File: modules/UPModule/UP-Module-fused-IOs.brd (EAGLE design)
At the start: 48.6 x 50.4 mm, 137 parts, among them IC1 LPC1115, IC100 BD9G101, IC2 ESDA5V3L, IC302 ESDA5V3L, IC303 ESDA5V3L, IC304 ESDA5V3L, IC401 ESDA5V3L, IC402 ESDA5V3L, IC403 ESDA5V3L, IC404 ESDA5V3L, Q2 ASFL, T1 BC856, T2 BCP52, T3 BC847, X1 EIB, X2 B7B-PH-K-S, X3 B8B-PH-K-S

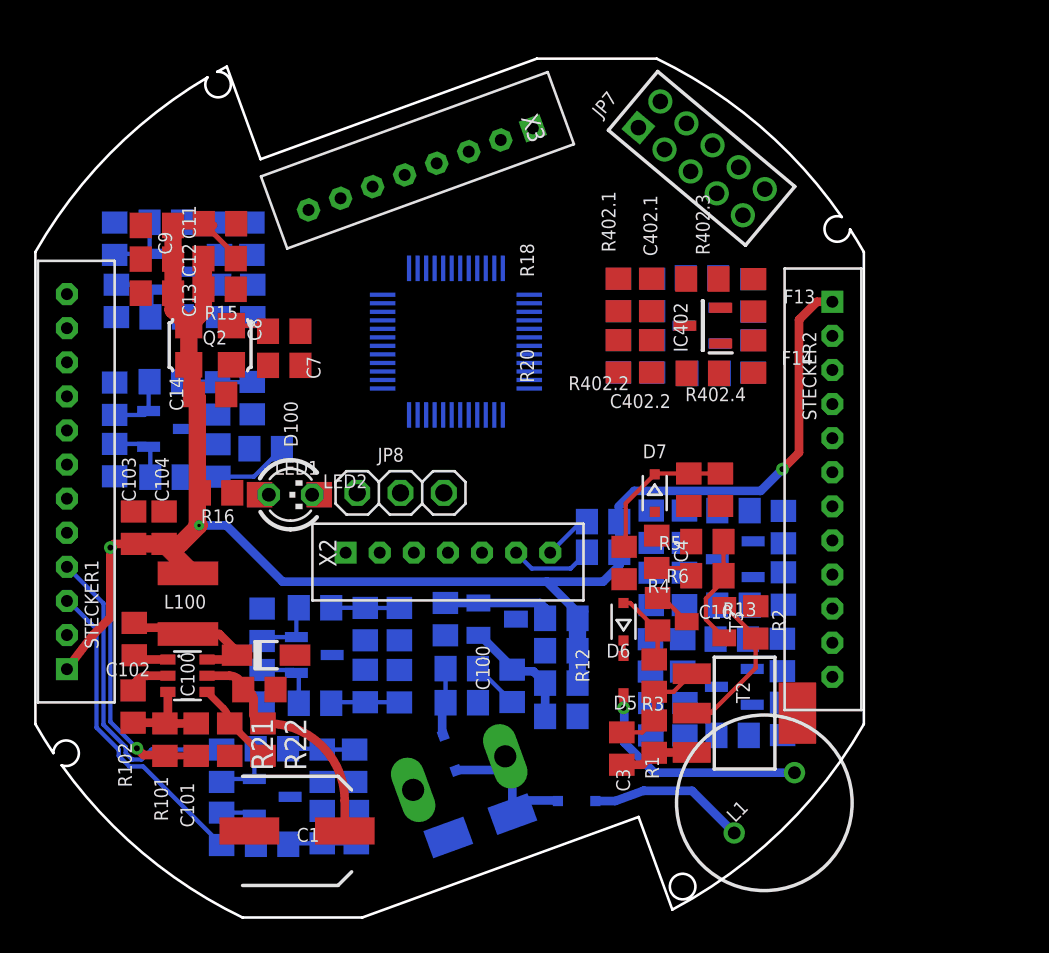
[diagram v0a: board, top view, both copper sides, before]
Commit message: Update of UP Module with fused IOs
Completely changed how IOs will be protected. EEPROM and cropty IC added.
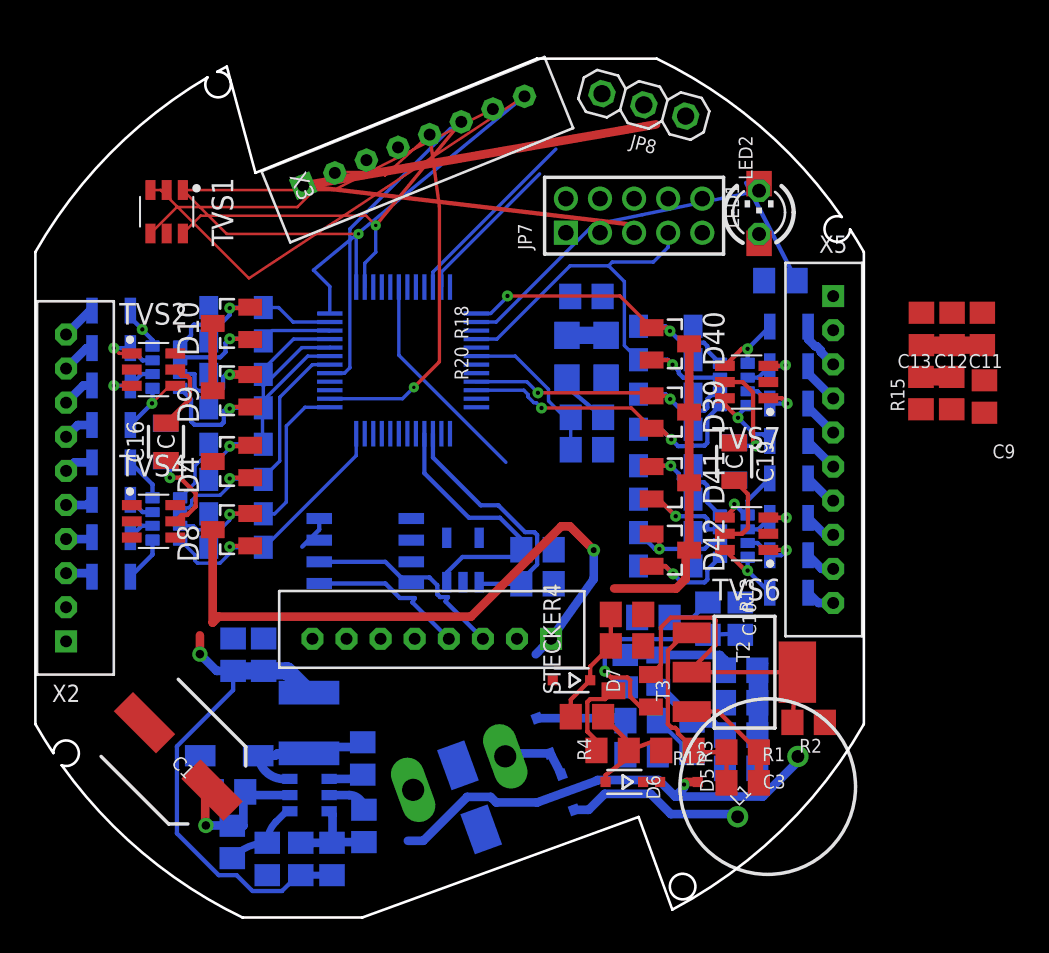
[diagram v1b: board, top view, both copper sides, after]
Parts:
- removed C302.1, C302.2, C303.1, C303.2, C304.1, C304.2, C304.3, C304.4, C401.1, C401.2, C402.1, C402.2, C403.1, C403.2, C404.1, C404.2: 10nF/50V, rcl:C0805
- removed F13, F14, F15, F16, F3, F4, F5: BSMD0805-005-33V, rcl:R0805
- removed IC2, IC302, IC303, IC304, IC401, IC402, IC403, IC404: ESDA5V3L, SamacSys_Parts:SOT105P242X150-3N
- removed R302.1, R302.2, R303.1, R303.2, R304.1, R304.2, R304.5, R304.6, R401.1, R401.2, R402.1, R402.2, R403.1, R403.2, R404.1, R404.2: 1M, rcl:R0805
- removed R302.3, R302.4, R303.3, R303.4, R304.3, R304.4, R304.7, R304.8, R401.3, R401.4, R402.3, R402.4, R403.3, R403.4, R404.3, R404.4: 1k, rcl:R0805
- removed STECKER1, STECKER2: B12B-PH-K-S, con-JST PH:B12B-PH-K-S
- added C16, C17, C19, C20: 100nF, MyRCL:C0805
- added D10, D39, D4, D40, D41, D42, D8, D9: BAT54C, diode:SOT23
- added D13, D14, D15, D16, D18, D19, D20, D21, D31, D32, D33, D34, D35, D36, D37, D38: DDZ9684 (3V3), Diode:SODFL3718X115
- added F1, F19, F20, F21, F22, F23, F24: (no value), MyFuse:F0805
- added IC5: ATAES132A-SHEQ-T, SamacSys_Parts:SOIC127P600X175-8N
- added R19, R23, R25, R26: YC164-JR-0733RL, Resistor Array:YC164-JR-0733RL
- added STECKER4: B8B-PH-K-S, con-JST PH:B8B-PH-K-S
- added TVS1, TVS2, TVS4, TVS6, TVS7: USBLC6-4SC6, usblc6:SOT-23-6L
- added U1: (no value), microbuilder:SOT23-5
- added X5: B10B-PH-KL, con-JST PH:B10B-PH-K-S
- F10, F11, F12, F17, F18, F6, F7, F8, F9: value BSMD0805-005-33V -> (none); device rcl:R0805 -> MyFuse:F0805
- X2: value B7B-PH-K-S -> B10B-PH-KL; device con-JST PH:B7B-PH-K-S -> con-JST PH:B10B-PH-K-S
- moved C11 48.8 mm to (55.4, 34.7), turned to 270 degrees
- moved C12 46.8 mm to (53.6, 34.7), turned to 270 degrees
- moved C9 46.0 mm to (55.5, 30.8), turned to 270 degrees
- moved C13 44.9 mm to (51.8, 34.7), turned to 270 degrees
- moved R14 43.7 mm to (53.5, 31.0), turned to 90 degrees
- moved R15 41.6 mm to (51.8, 31.0), turned to 90 degrees
- moved F11 39.5 mm to (4.25, 24.7), turned to 180 degrees
- moved F12 38.2 mm to (4.25, 26.9), turned to 180 degrees
- moved R16 35.4 mm to (43.5, 37.6), flipped to the bottom
- moved LED1 32.1 mm to (42.3, 41.5), turned to 0 degrees
- moved LED2 32.1 mm to (42.2, 41.6), turned to 90 degrees
- moved F7 28.9 mm to (4.25, 33.6), turned to 180 degrees
- moved F8 27.5 mm to (4.25, 35.8), turned to 180 degrees
- moved JP8 26.9 mm to (35.5, 47.9), turned to 165 degrees
- moved C14 22.8 mm to (32.1, 36.6), flipped to the bottom
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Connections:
- removed net C1_P10: F10.2, STECKER1.10
- removed net C1_P10_F: F10.1, IC2.2, R304.8.1
- removed net C1_P3: F7.2, STECKER1.3
- removed net C1_P3_F: F7.1, IC304.1, R304.3.1
- removed net C1_P4: F8.2, STECKER1.4
- removed net C1_P4_F: F8.1, IC304.2, R304.4.1
- removed net C1_P5: F5.2, STECKER1.5
- removed net C1_P5_F: F5.1, IC303.1, R303.3.1
- removed net C1_P6: F6.2, STECKER1.6
- removed net C1_P6_F: F6.1, IC303.2, R303.4.1
- removed net C1_P7: F4.2, STECKER1.7
- removed net C1_P7_F: F4.1, IC302.1, R302.4.1
- removed net C1_P8: F3.2, STECKER1.8
- removed net C1_P8_F: F3.1, IC302.2, R302.3.1
- removed net C1_P9: F9.2, STECKER1.9
- removed net C1_P9_F: F9.1, IC2.1, R304.7.1
- removed net C2_P10: F18.2, STECKER2.10
- removed net C2_P10_F: F18.1, IC404.1, R404.4.1
- removed net C2_P3: F11.2, STECKER2.3
- removed net C2_P3_F: F12.1, IC401.1, R401.4.1
- removed net C2_P4: F12.2, STECKER2.4
- removed net C2_P4_F: F11.1, IC401.2, R401.3.1
- removed net C2_P5: F14.2, STECKER2.5
- removed net C2_P5_F: F14.1, IC402.1, R402.4.1
- removed net C2_P6: F13.2, STECKER2.6
- removed net C2_P6_F: F13.1, IC402.2, R402.3.1
- removed net C2_P7: F15.2, STECKER2.7
- removed net C2_P7_F: F15.1, IC403.1, R403.3.1
- removed net C2_P8: F16.2, STECKER2.8
- removed net C2_P8_F: F16.1, IC403.2, R403.4.1
- removed net C2_P9: F17.2, STECKER2.9
- removed net C2_P9_F: F17.1, IC404.2, R404.3.1
- removed net EIB_IN: C5.2, IC1.9, R7.1, T1.E
- removed net IO1: C304.2.2, IC1.12, R304.1.2, R304.3.2
- removed net IO10: C401.1.2, IC1.26, R401.1.2, R401.3.2
- removed net IO11: C402.1.2, IC1.27, R402.1.2, R402.3.2
- removed net IO12: C402.2.2, IC1.28, R402.2.2, R402.4.2
- removed net IO13: C403.1.2, IC1.35, R403.1.2, R403.3.2
- removed net IO16: C404.2.2, IC1.34, R404.2.2, R404.4.2
- removed net IO17: IC1.15, R18.1, X2.7
- removed net IO18: IC1.16, R20.1, X2.6
- removed net IO2: C304.1.2, IC1.14, R304.2.2, R304.4.2
- removed net IO7: C304.3.2, IC1.20, R304.5.2, R304.7.2
- removed net IO8: C304.4.2, IC1.21, R304.6.2, R304.8.2
- removed net IO9: C401.2.2, IC1.25, R401.2.2, R401.4.2
- removed net ISP_EN: IC1.4, JP7.7, R15.1
- new net IN1: F9.1, X2.3
- new net IN10: F22.1, X5.4
- new net IN11: F23.1, X5.5
- new net IN12: F24.1, X5.6
- new net IN13: F17.1, X5.7
- new net IN14: F18.1, X5.8
- new net IN15: F19.1, X5.9
- new net IN16: F20.1, X5.10
- new net IN2: F10.1, X2.4
- new net IN3: F11.1, X2.5
- new net IN4: F12.1, X2.6
- new net IN5: F1.1, X2.7
- new net IN6: F6.1, X2.8
- new net IN7: F7.1, X2.9
- new net IN8: F8.1, X2.10
- new net IN9: F21.1, X5.3
- new net IO107: D13.1, D9.1, IC1.32, R19.8
- new net IO108: D14.1, D9.2, IC1.33, R19.7
- new net IO109: D10.1, D15.1, IC1.34, R19.6
- new net IO11/MISO0: IC1.27
- new net IO110: D10.2, D16.1, IC1.35, R19.5
- new net IO113: C5.2, D35.1, D39.1, IC1.9, R26.6, R7.1, T1.E
- new net IO114: D36.1, D39.2, IC1.10, R26.5
- new net IO115: D37.1, D40.1, IC1.1, R26.8
- new net IO117: D31.1, D41.1, R25.8
- new net IO118: D32.1, D41.2, R25.7
- new net IO119: D33.1, D42.1, R25.6
- new net IO12/MOSI0: IC1.28
- new net IO120: D34.1, D42.2, R25.5
- new net IO17/SCL: IC1.15, IC5.6, R18.1, STECKER4.3, U1.1
- new net IO18/SDA: IC1.16, IC5.5, R20.1, STECKER4.4, U1.3
- new net ISP_EN/IO116: D38.1, D40.2, IC1.4, JP7.7, R15.1, R26.7
- new net MISO1: IC1.26, TVS1.4, X3.5
- new net MOSI1: IC1.38, TVS1.6, X3.6
- new net N$18: F1.2, R19.1, TVS2.4
- new net N$19: F6.2, R19.2, TVS2.3
- new net N$20: F7.2, R19.3, TVS2.1
- new net N$21: F8.2, R19.4, TVS2.6
- new net N$22: C16.2, TVS2.5
- new net N$23: F10.2, R23.2, TVS4.3
- new net N$24: F12.2, R23.4, TVS4.6
- new net N$25: C17.2, TVS4.5
- new net N$26: F11.2, R23.3, TVS4.1
- new net N$27: F9.2, R23.1, TVS4.4
- new net N$33: F18.2, R25.2, TVS6.3
- new net N$34: F20.2, R25.4, TVS6.6
- new net N$35: C19.2, TVS6.5
- new net N$36: F19.2, R25.3, TVS6.1
- new net N$37: F17.2, R25.1, TVS6.4
- new net N$38: F22.2, R26.2, TVS7.3
- new net N$39: F24.2, R26.4, TVS7.6
- new net N$40: C20.2, TVS7.5
- new net N$42: F23.2, R26.3, TVS7.1
- new net N$43: F21.2, R26.1, TVS7.4
- new net RXD: IC1.11, IC1.37, TVS1.1, X3.7
- new net TXD: IC1.12, IC1.36, TVS1.3, X3.8
- new net XTALOUT: IC1.7
- net +3V3: now also D10.3, D39.3, D4.3, D40.3, D41.3, D42.3, D8.3, D9.3, IC5.8, STECKER4.1, U1.4, U1.5, X2.1, X3.1, X5.1; no longer STECKER1.1, STECKER2.1
- net GND: now also C16.1, C17.1, C19.1, C20.1, D13.2, D14.2, D15.2, D16.2, D18.2, D19.2, D20.2, D21.2, D31.2, D32.2, D33.2, D34.2, D35.2, D36.2, D37.2, D38.2, IC5.4, STECKER4.2, TVS1.2, TVS2.2, TVS4.2, TVS6.2, TVS7.2, U1.2, X2.2, X3.2, X5.2; no longer C302.1.1, C302.2.1, C303.1.1, C303.2.1, C304.1.1, C304.2.1, C304.3.1, C304.4.1, C401.1.1, C401.2.1, C402.1.1, C402.2.1, C403.1.1, C403.2.1, C404.1.1, C404.2.1, IC2.3, IC302.3, IC303.3, IC304.3, IC401.3, IC402.3, IC403.3, IC404.3, R302.1.1, R302.2.1, R303.1.1, R303.2.1, R304.1.1, R304.2.1, R304.5.1, R304.6.1, R401.1.1, R401.2.1, R402.1.1, R402.2.1, R403.1.1, R403.2.1, R404.1.1, R404.2.1, STECKER1.2, STECKER2.2
- net IO14: now also IC1.13; no longer C403.2.2, IC1.36, R403.2.2, R403.4.2
- net IO15: now also IC1.14; no longer C404.1.2, IC1.33, R404.1.2, R404.3.2
- net IO3: now also D20.1, D8.1, IC1.24, R23.8; no longer C303.1.2, IC1.10, R303.1.2, R303.3.2
- net IO4: now also D21.1, D8.2, IC1.25, R23.7; no longer C303.2.2, IC1.13, R303.2.2, R303.4.2
- net IO5: now also D18.1, D4.1, IC1.30, R23.6; no longer C302.2.2, IC1.11, R302.2.2, R302.4.2
- net IO6: now also D19.1, D4.2, IC1.31, R23.5; no longer C302.1.2, IC1.1, R302.1.2, R302.3.2
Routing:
- net TXD: track 0.00 -> 46.3 mm
- net +3V3: track 115.5 -> 156.9 mm, vias 4 -> 2
- net MISO1: track 0.00 -> 39.6 mm, vias 0 -> 1
- net RXD: track 0.00 -> 33.9 mm, vias 0 -> 1
- net IO17/SCL: track 0.00 -> 27.3 mm
- net ISP_EN/IO116: track 0.00 -> 27.2 mm, vias 0 -> 1
- net IO18/SDA: track 0.00 -> 25.0 mm
- net IO113: track 0.00 -> 24.4 mm, vias 0 -> 2
- net MOSI1: track 0.00 -> 23.7 mm, vias 0 -> 1
- net IO114: track 0.00 -> 19.7 mm, vias 0 -> 2
- net PROG: track 0.00 -> 19.1 mm
- net C1_P3: track 18.6 -> 0.00 mm
- net IO115: track 0.00 -> 18.5 mm, vias 0 -> 2
- net C1_P4: track 18.4 -> 0.00 mm
- net SWCLK: track 0.00 -> 17.8 mm
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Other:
- outline, holes or cut-outs redrawn
- board text removed: "+3V3 Power Supply Buck Converter"
- board text removed: "Connector 2"
- board text removed: "EIB Out Circuit"
- board text removed: "EIB in Circuit"
- board text removed: "High precision 12 MHz Clock"
- board text removed: "Pin 1.3 + 1.4 Protection"
- board text removed: "Pin 2.3 + 2.4 Protection"
- board text removed: "Pin 2.7 + 2.8 Protection"
- board text removed: "Pins 1.3 + 1.4 Protection"
- board text removed: "Pins 1.7 + 1.8 Protection"
- board text removed: "Pins 1.9 + 1.10 Protection"
- board text removed: "Pins 2.5 + 2.6 Protection"
- board text removed: "Pins 2.9 + 2.10 Protection"
- board text removed: "Reverse Voltage & Over Voltage protection"

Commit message: UP Module with fused IOs: alpha version
routing of a version with max. IOs / functions fitting on a single PCB for in-wall installation done. Parts size 0805.
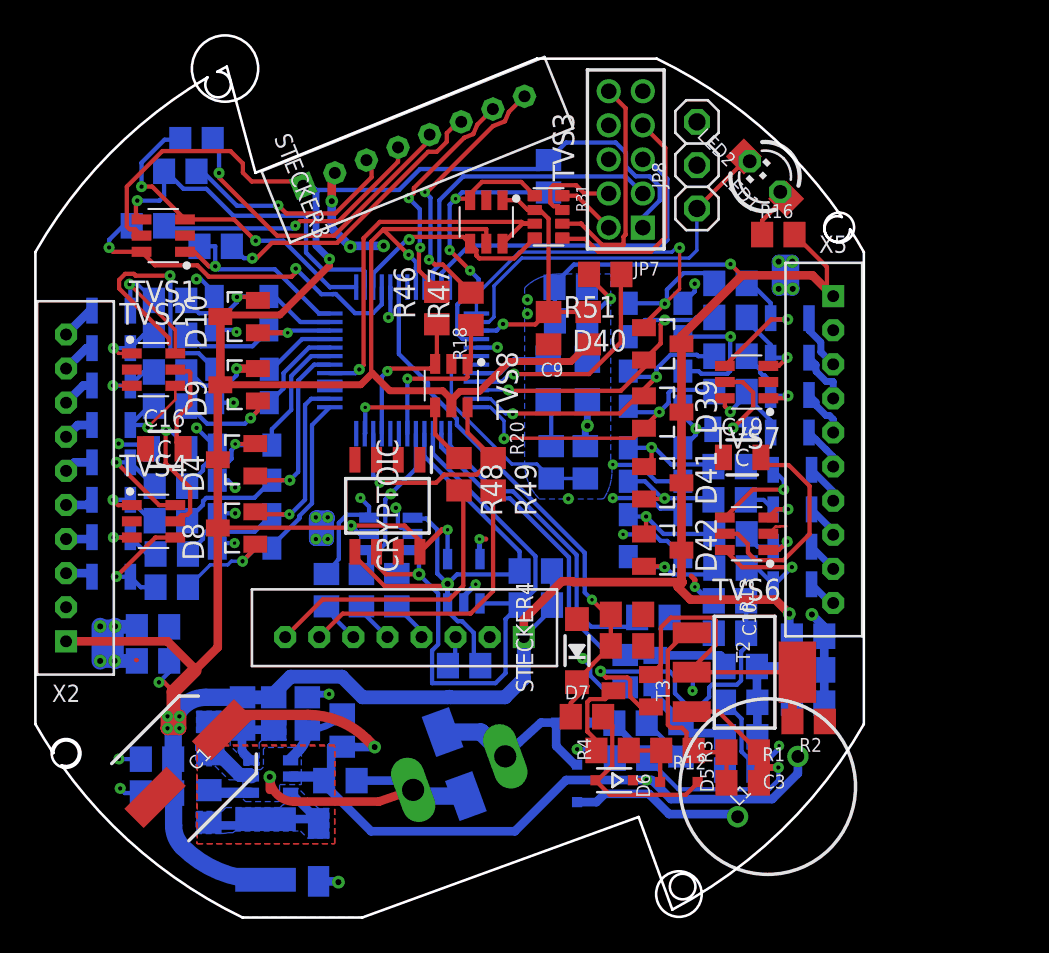
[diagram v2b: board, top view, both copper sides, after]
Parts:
- removed IC5: ATAES132A-SHEQ-T, SamacSys_Parts:SOIC127P600X175-8N
- added C15, C18: 100n, rcl:C0805
- added CRYPTOIC: ATAES132A-SHER-B, SamacSys_Parts:SOIC127P600X175-8N
- added R17, R24, R27, R28, R29, R30, R40, R41, R42, R43, R44, R45: (no value), rcl:R0805
- added R31: 1k, Resistor Array:YC164-JR-0733RL
- added R32, R34: 33R, rcl:R0805
- added R33, R35, R36, R37: 100R, rcl:R0805
- added R38, R39, R48, R49: 1k, rcl:R0805
- added R46, R47: 1K, rcl:R0805
- added R50: 100k, rcl:R0805
- added R51: 0R0, rcl:R0805
- added TVS3, TVS5, TVS8: USBLC6-4SC6, usblc6:SOT-23-6L
- D7: value 3V6 -> DDZ9685 -option; device diode:SOD323-R -> microbuilder:SOD-123
- R12: value 91k -> 43k
- R13: value 10k -> 6,2k
- R19, R23, R25, R26: value YC164-JR-0733RL -> (none); device Resistor Array:YC164-JR-0733RL -> rcl:R0805
- U1: value (none) -> EEPROM
- moved C9 25.9 mm to (29.9, 34.8), turned to 90 degrees
- moved R15 25.3 mm to (29.9, 43.7), flipped to the bottom
- moved C11 24.2 mm to (45.1, 12.8), flipped to the bottom, turned to 0 degrees
- moved R14 21.7 mm to (32.2, 34.8), turned to 270 degrees
- moved C13 21.1 mm to (45.1, 14.7), flipped to the bottom, turned to 0 degrees
- moved C12 19.9 mm to (45.1, 16.7), flipped to the bottom, turned to 0 degrees
- moved R102 10.4 mm to (9.98, 10.7), turned to 90 degrees
- moved R101 10.0 mm to (11.9, 12.2), turned to 90 degrees
- moved C102 9.45 mm to (9.97, 6.72), turned to 90 degrees
- moved C104 9.26 mm to (6.93, 7.50), turned to 0 degrees
- moved R22 9.18 mm to (17.8, 11.2), turned to 90 degrees
- moved R21 8.85 mm to (15.8, 12.2), turned to 90 degrees
- moved C103 8.76 mm to (6.93, 9.49), turned to 0 degrees
- moved C101 8.68 mm to (13.8, 12.2), turned to 90 degrees
- moved L100 7.84 mm to (13.3, 4.19), turned to 270 degrees
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- renumbered X3 to STECKER3
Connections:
- net N$4 renamed XTALIN
- removed net IO14: IC1.13
- removed net IO15: IC1.14
- removed net ISP_EN/IO116: D38.1, D40.2, IC1.4, JP7.7, R15.1, R26.7
- removed net RXD: IC1.11, IC1.37, STECKER3.7, TVS1.1
- removed net TXD: IC1.12, IC1.36, STECKER3.8, TVS1.3
- new net EIB_IN: C5.2, IC1.14, R7.1, T1.E
- new net IN200: R38.2, STECKER3.4
- new net IN201: R39.2, STECKER3.3
- new net IN_MISO1: R35.2, STECKER4.6
- new net IN_MOSI1: R33.2, STECKER4.5
- new net IO116: D38.1, D40.2, IC1.10, R43.2
- new net IO19: IC1.18, R47.1, TVS8.1
- new net IO20: IC1.21, R46.1, TVS8.3
- new net IO200: IC1.38, R39.1, TVS1.4
- new net IO201: IC1.40, R38.1, TVS1.6
- new net IO21: IC1.22, R49.1, TVS8.6
- new net IO22: IC1.23, R48.1, TVS8.4
- new net ISP_EN: IC1.4, R15.1, R31.1, TVS3.3
- new net N$11: JP7.10, R31.6
- new net N$13: JP7.4, R31.7
- new net N$16: R34.2, STECKER4.4
- new net N$28: Q2.1, R50.1, R51.2
- new net N$29: R36.2, STECKER3.5
- new net N$30: R37.2, STECKER3.6
- new net N$47: R47.2, STECKER3.8
- new net N$48: R46.2, STECKER3.7
- new net N$49: R49.2, STECKER4.7
- new net N$52: R48.2, STECKER4.8
- new net N$8: JP7.7, R31.5
- new net OLD_REF: D5.C, R3.1, R4.2
- new net RXD2: IC1.37, R36.1, TVS1.3
- new net SWD_SWDIO: JP7.2, R31.8
- new net TXD2: IC1.36, R37.1, TVS1.1
- new net XTAL_EN: IC1.9, R51.1
- net +3V3: now also C15.1, C18.1, CRYPTOIC.8, R50.2, TVS1.5, TVS3.5, TVS5.5, TVS8.5; no longer IC5.8, Q2.1, U1.5
- net EIB_DC: now also D6.C; no longer D5.A
- net EIB_OUT: now also IC1.13; no longer IC1.17
- net GND: now also C15.2, C18.2, CRYPTOIC.1, CRYPTOIC.4, TVS3.2, TVS5.2, TVS8.2, U1.5; no longer IC5.4
- net IO107: now also R17.2; no longer R19.8
- net IO108: now also R19.2; no longer R19.7
- net IO109: now also R24.2; no longer R19.6
- net IO110: now also R27.2; no longer R19.5
- net IO113: now also IC1.11, R44.2; no longer C5.2, IC1.9, R26.6, R7.1, T1.E
- net IO114: now also IC1.12, R45.2; no longer IC1.10, R26.5
- net IO115: now also R26.2; no longer R26.8
- net IO117: now also R42.2; no longer R25.8
- net IO118: now also R41.2; no longer R25.7
- net IO119: now also R40.2; no longer R25.6
- net IO120: now also R25.2; no longer R25.5
- net IO17/SCL: now also CRYPTOIC.6, R34.1, TVS5.3; no longer IC5.6, STECKER4.3
- net IO18/SDA: now also CRYPTOIC.5, R32.1, TVS5.1; no longer IC5.5, STECKER4.4
- net IO3: now also IC1.25, R23.2; no longer IC1.24, R23.8
- net IO4: now also IC1.26, R28.2; no longer IC1.25, R23.7
- net IO5: now also R29.2; no longer R23.6
- net IO6: now also R30.2; no longer R23.5
- net MISO1: now also R35.1, TVS5.6; no longer IC1.26, STECKER3.5, TVS1.4
- net MOSI1: now also IC1.17, R33.1, TVS5.4; no longer IC1.38, STECKER3.6, TVS1.6
- net N$18: now also R17.1; no longer R19.1
- net N$19: now also R19.1; no longer R19.2
- net N$20: now also R24.1; no longer R19.3
- net N$21: now also R27.1; no longer R19.4
- net N$23: now also R28.1; no longer R23.2
- net N$24: now also R30.1; no longer R23.4
- net N$26: now also R29.1; no longer R23.3
- net N$33: now also R41.1; no longer R25.2
- net N$34: now also R25.1; no longer R25.4
- net N$36: now also R40.1; no longer R25.3
- net N$37: now also R42.1; no longer R25.1
- net N$38: now also R43.1; no longer R26.2
- net N$39: now also R45.1; no longer R26.4
- net N$42: now also R44.1; no longer R26.3
- net N$9: now also R32.2, STECKER4.3; no longer D5.C, D6.C
- net REF: now also D5.A; no longer R3.1, R4.2
- net RESET: now also R31.2, TVS3.1; no longer JP7.10
- net SWCLK: now also R31.3, TVS3.6; no longer JP7.4
- net SWDIO: now also R31.4, TVS3.4; no longer JP7.2
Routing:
- net GND: track 2.40 -> 137.1 mm, vias 0 -> 50
- net +3V3: track 156.9 -> 287.1 mm, vias 2 -> 11
- net TXD: track 46.3 -> 0.00 mm
- net RXD: track 33.9 -> 0.00 mm, vias 1 -> 0
- net MISO1: track 39.6 -> 6.68 mm
- net ISP_EN/IO116: track 27.2 -> 0.00 mm, vias 1 -> 0
- net EIB_IN: track 0.00 -> 25.1 mm
- net ISP_EN: track 0.00 -> 21.8 mm, vias 0 -> 3
- net IO201: track 0.00 -> 21.5 mm, vias 0 -> 2
- net IO200: track 0.00 -> 20.8 mm, vias 0 -> 1
- net IO116: track 0.00 -> 19.7 mm, vias 0 -> 2
- net RXD2: track 0.00 -> 19.3 mm, vias 0 -> 2
- net N$29: track 0.00 -> 19.0 mm, vias 0 -> 1
- net EIB_OUT: track 0.00 -> 18.3 mm
- net N$52: track 0.00 -> 17.4 mm
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- added copper zone on layer 1, net ARGL
- added copper zone on layer 16, net FB
- added copper zone on layer 1, net GND
- added copper zone on layer 16, net GND
- added copper zone on layer 16, net LX
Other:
- board size 48.6 x 50.4 mm -> 48.6 x 51.7 mm
